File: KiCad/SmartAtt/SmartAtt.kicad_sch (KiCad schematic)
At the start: 11 parts, among them IC1 74LVC4245APW,112, J1 Conn_01x02_Pin, J2 Conn_01x02_Pin, J3 Conn_01x02_Pin, J4 Conn_01x04_Pin, U1 ESP32-WROOM-32E, U2 HMC542BLP4ETR, U3 MCP1703Ax-330xxDB

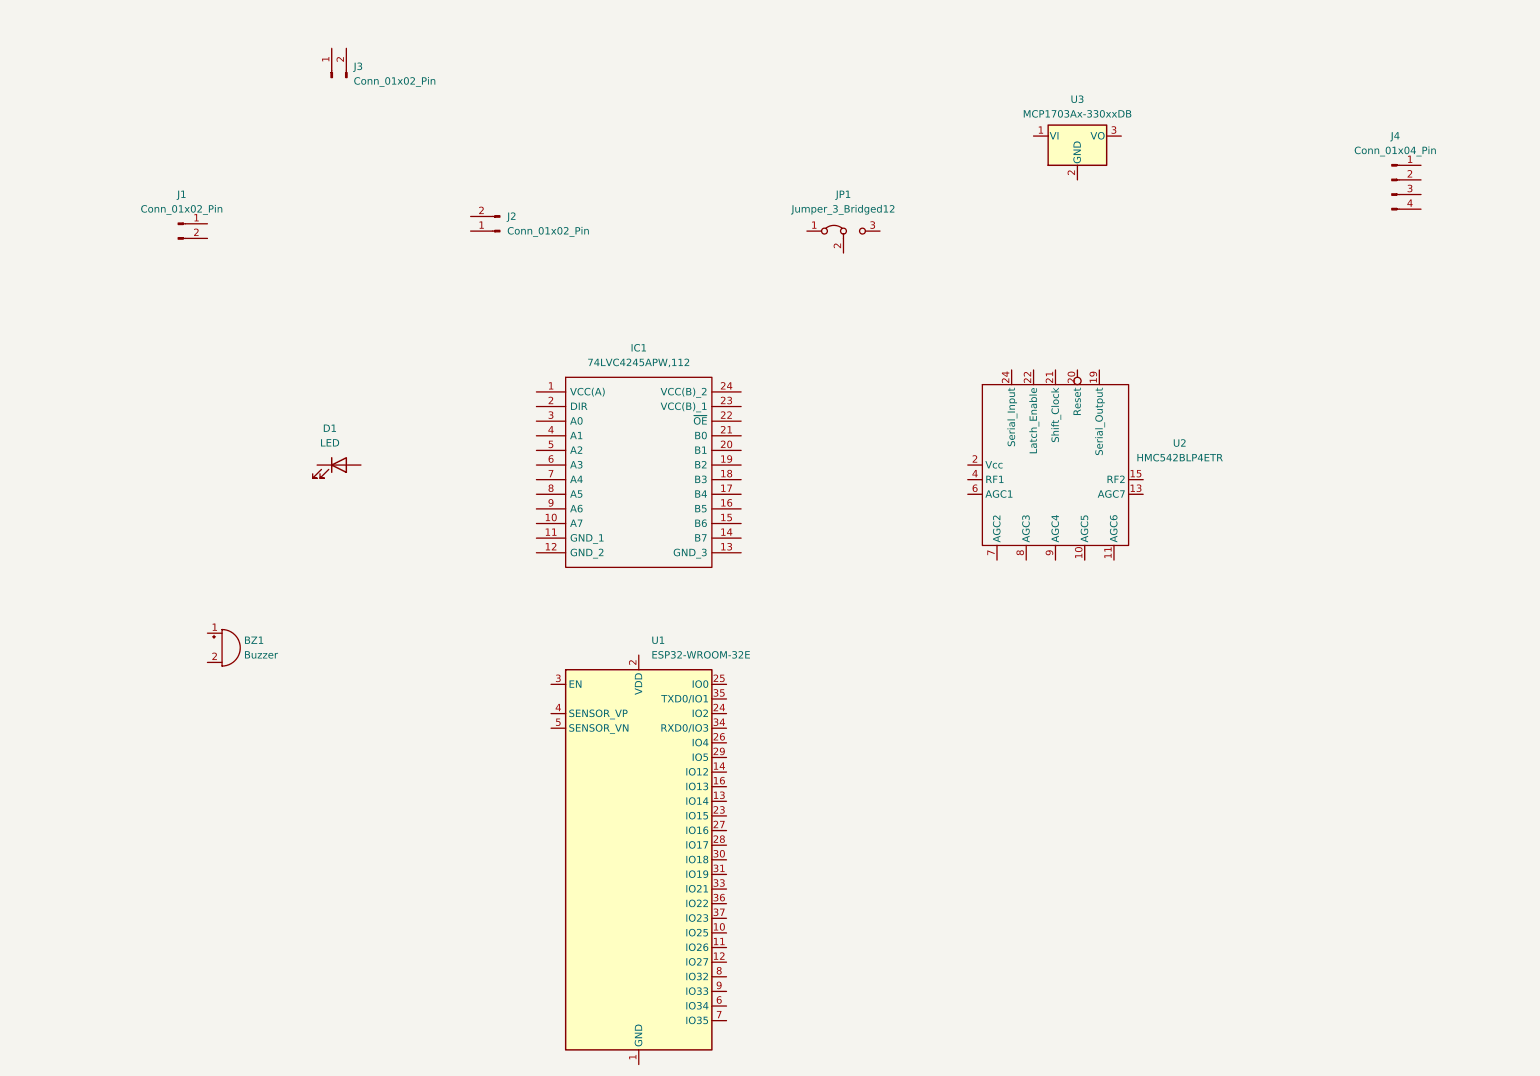
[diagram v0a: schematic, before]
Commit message: schematic finished. Need footprint to be added
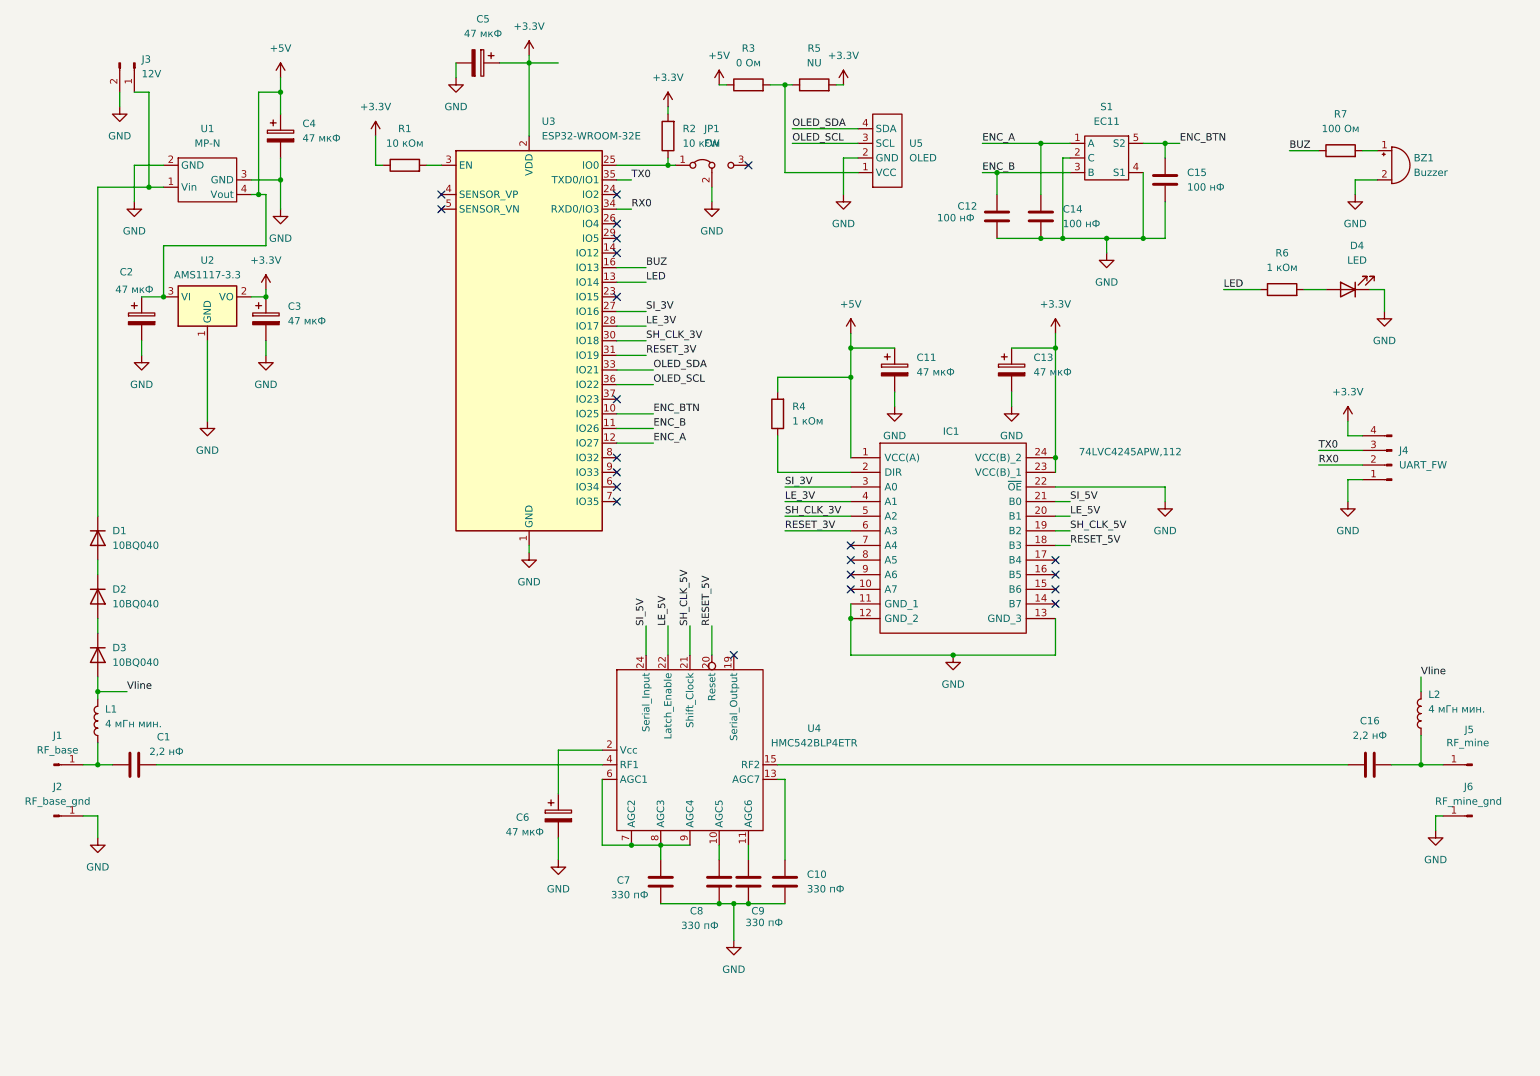
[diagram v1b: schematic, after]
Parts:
- removed J1, J2: Conn_01x02_Pin, symbol Connector:Conn_01x02_Pin
- removed U3: MCP1703Ax-330xxDB, Package_TO_SOT_SMD:SOT-223-3_TabPin2, symbol Regulator_Linear:MCP1703Ax-330xxDB
- added C1, C16: 2,2 нФ, symbol Device:C
- added C10, C7, C8, C9: 330 пФ, symbol Device:C
- added C11, C13, C2, C3, C4, C5, C6: 47 мкФ, symbol Device:C_Polarized
- added C12, C14, C15: 100 нФ, symbol Device:C
- added D1, D2, D3: 10BQ040, symbol Device:D
- added J1: RF_base, symbol Connector:Conn_01x01_Pin
- added J2: RF_base_gnd, symbol Connector:Conn_01x01_Pin
- added J5: RF_mine, symbol Connector:Conn_01x01_Pin
- added J6: RF_mine_gnd, symbol Connector:Conn_01x01_Pin
- added L1, L2: 4 мГн мин., symbol Device:L
- added R1, R2: 10 кОм, symbol Device:R
- added R3: 0 Ом, symbol Device:R
- added R4, R6: 1 кОм, symbol Device:R
- added R5: NU, symbol Device:R
- added R7: 100 Ом, symbol Device:R
- added S1: EC11, symbol Alexeyj4_Library:EC11_rotary_encoder
- added U1: MP-N, symbol Alexeyj4_Library:MPN
- added U2: AMS1117-3.3, Package_TO_SOT_SMD:SOT-223-3_TabPin2, symbol Regulator_Linear:AMS1117-3.3
- added U5: OLED, symbol Alexeyj4_Library:OLED I2C
- IC1: symbol Shar_Library:74LVC4245APW,112 -> Alexeyj4_Library:74LVC4245APW,112
- J3: value Conn_01x02_Pin -> 12V
- J4: value Conn_01x04_Pin -> UART_FW
- JP1: value Jumper_3_Bridged12 -> FW
- U4: renamed from U2; symbol Shar_Library:HMC542BLP4ETR -> Alexeyj4_Library:HMC542BLP4ETR
- renumbered D1 to D4, U1 to U3
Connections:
- net at BZ1.1 (+): now also R7.2
- net GND: now reaches BZ1.2 (-)
- net GND: now also D4.1 (K), IC1.11 (GND_1), IC1.12 (GND_2), IC1.13 (GND_3), IC1.22 (~{OE}), J3.2 (Pin_2), J4.1 (Pin_1), JP1.2 (C), U3.1 (GND), U3.15 (GND), U3.38 (GND), U3.39 (GND), C10.2, C11.2, C12.2, C13.2, C14.2, C15.2, C2.2, C3.2, C4.2, C5.2, C6.2, C7.2, C8.2, C9.2, J2.1 (Pin_1), J6.1 (Pin_1), S1.2 (C), S1.4 (S1), U1.2 (GND), U1.3 (GND), U2.1 (GND), U5.2 (GND)
- net at J3.1 (Pin_1): now also D1.1 (K), U1.1 (Vin)
- net RX0: now reaches J4.2 (Pin_2)
- net RX0: now also U3.34 (RXD0/IO3)
- net TX0: now reaches J4.3 (Pin_3)
- net TX0: now also U3.35 (TXD0/IO1)
- net +3.3V: now reaches J4.4 (Pin_4)
- net +3.3V: now also IC1.23 (VCC(B)_1), IC1.24 (VCC(B)_2), U3.2 (VDD), C13.1, C3.1, C5.1, R1.1, R2.2, R5.2, U2.2 (VO)
- net ENC_BTN: now reaches U3.10 (IO25)
- net ENC_BTN: now also C15.1, S1.5 (S2)
- net ENC_B: now reaches U3.11 (IO26)
- net ENC_B: now also C12.1, S1.3 (B)
- net ENC_A: now reaches U3.12 (IO27)
- net ENC_A: now also C14.1, S1.1 (A)
- net LED: now reaches U3.13 (IO14)
- net LED: now also R6.1
- net BUZ: now reaches U3.16 (IO13)
- net BUZ: now also R7.1
- net at U3.25 (IO0): now also JP1.1 (A), R2.1
- net SI_3V: now reaches U3.27 (IO16)
- net SI_3V: now also IC1.3 (A0)
- net LE_3V: now reaches U3.28 (IO17)
- net LE_3V: now also IC1.4 (A1)
- net at U3.3 (EN): now also R1.2
- net SH_CLK_3V: now reaches U3.30 (IO18)
- net SH_CLK_3V: now also IC1.5 (A2)
- net RESET_3V: now reaches U3.31 (IO19)
- net RESET_3V: now also IC1.6 (A3)
- net OLED_SDA: now reaches U3.33 (IO21)
- net OLED_SDA: now also U5.4 (SDA)
- net OLED_SCL: now reaches U3.36 (IO22)
- net OLED_SCL: now also U5.3 (SCL)
- net at D4.2 (A): now also R6.2
- net +5V: now reaches IC1.1 (VCC(A))
- net +5V: now also C11.1, C2.1, C4.1, R3.1, R4.2, U1.4 (Vout), U2.3 (VI)
- net RESET_5V: now reaches IC1.18 (B3)
- net RESET_5V: now also U4.20 (Reset)
- net SH_CLK_5V: now reaches IC1.19 (B2)
- net SH_CLK_5V: now also U4.21 (Shift_Clock)
- net at IC1.2 (DIR): now also R4.1
- net LE_5V: now reaches IC1.20 (B1)
- net LE_5V: now also U4.22 (Latch_Enable)
- net SI_5V: now reaches IC1.21 (B0)
- net SI_5V: now also U4.24 (Serial_Input)
- net at U4.10 (AGC5): now also C8.1
- net at U4.11 (AGC6): now also C9.1
- net at U4.13 (AGC7): now also C10.1
- net at U4.15 (RF2): now also C16.2
- net at U4.2 (Vcc): now also C6.1
- net at U4.4 (RF1): now also C1.1
- net at U4.6 (AGC1): now also U4.7 (AGC2), U4.8 (AGC3), U4.9 (AGC4), C7.1
- new net: D1.2 (A), D2.1 (K)
- new net: D2.2 (A), D3.1 (K)
- new net: C1.2, J1.1 (Pin_1), L1.1
- new net: C16.1, J5.1 (Pin_1), L2.1
- new net: R3.2, R5.1, U5.1 (VCC)
- new net Vline: D3.2 (A), L1.2, L2.2
- no-connect marks 0 -> 22
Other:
- moved on the sheet: BZ1, D4, IC1, J4, JP1, U3, U4

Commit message: contur added
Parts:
- BZ1: footprint (none) -> Alexeyj4:HC0903A
- C1, C16: footprint (none) -> Capacitor_THT:C_Disc_D10.0mm_W2.5mm_P5.00mm
- C10, C12, C14, C15, C7, C8, C9: footprint (none) -> Capacitor_SMD:C_0805_2012Metric_Pad1.18x1.45mm_HandSolder
- C11, C13, C2, C3, C4, C5, C6: footprint (none) -> Capacitor_Tantalum_SMD:CP_EIA-7343-31_Kemet-D_Pad2.25x2.55mm_HandSolder
- D1, D2, D3: footprint (none) -> Diode_SMD:D_SMB_Handsoldering
- D4: footprint (none) -> LED_SMD:LED_1206_3216Metric_Pad1.42x1.75mm_HandSolder
- J1, J2, J5, J6: footprint (none) -> TestPoint:TestPoint_Pad_1.0x1.0mm
- J3: footprint (none) -> Connector_JST:JST_PH_B2B-PH-K_1x02_P2.00mm_Vertical
- J4: footprint (none) -> Connector_PinHeader_2.54mm:PinHeader_1x04_P2.54mm_Vertical
- JP1: footprint (none) -> Connector_PinHeader_2.54mm:PinHeader_1x03_P2.54mm_Vertical
- L1, L2: footprint (none) -> Inductor_THT:L_Axial_L24.0mm_D7.1mm_P30.48mm_Horizontal_Vishay_IM-10-28
- R1, R2, R3, R4, R6, R7: footprint (none) -> Resistor_SMD:R_0805_2012Metric_Pad1.20x1.40mm_HandSolder
- R5: footprint (none) -> Resistor_SMD:R_0805_2012Metric_Pad1.20x1.40mm_HandSolder; now not fitted
- S1: footprint (none) -> Alexeyj4:RotaryEncoder EC11 SMD
- U1: footprint (none) -> Alexeyj4:MPN
- U5: footprint (none) -> Alexeyj4:OLED I2C
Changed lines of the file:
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@@
 			)
 		)
-		(property "Footprint" ""
+		(property "Footprint" "Capacitor_Tantalum_SMD:CP_EIA-7343-31_Kemet-D_Pad2.25x2.55mm_HandSolder"
 			(at 92.71 22.5552 0)
 			(effects
@@
 			)
 		)
-		(property "Footprint" ""
+		(property "Footprint" "Alexeyj4:HC0903A"
 			(at 254.635 36.83 90)
 			(effects
@@
 			)
 		)
-		(property "Footprint" ""
+		(property "Footprint" "Diode_SMD:D_SMB_Handsoldering"
 			(at 30.48 114.3 0)
 			(effects
@@
 			)
 		)
-		(property "Footprint" ""
+		(property "Footprint" "Resistor_SMD:R_0805_2012Metric_Pad1.20x1.40mm_HandSolder"
 			(at 246.38 38.608 90)
 			(effects
@@
 			)
 		)
-		(property "Footprint" ""
+		(property "Footprint" "Inductor_THT:L_Axial_L24.0mm_D7.1mm_P30.48mm_Horizontal_Vishay_IM-10-28"
 			(at 30.48 135.89 0)
 			(effects
@@
 			)
 		)
-		(property "Footprint" ""
+		(property "Footprint" "Resistor_SMD:R_0805_2012Metric_Pad1.20x1.40mm_HandSolder"
 			(at 236.22 62.738 90)
 			(effects
@@
 			)
 		)
-		(property "Footprint" ""
+		(property "Footprint" "Connector_PinHeader_2.54mm:PinHeader_1x04_P2.54mm_Vertical"
 			(at 255.27 91.44 0)
 			(effects
@@
 			)
 		)
-		(property "Footprint" ""
+		(property "Footprint" "Capacitor_Tantalum_SMD:CP_EIA-7343-31_Kemet-D_Pad2.25x2.55mm_HandSolder"
 			(at 169.8752 78.74 0)
 			(effects
@@
 			)
 		)
-		(property "Footprint" ""
+		(property "Footprint" "Capacitor_SMD:C_0805_2012Metric_Pad1.18x1.45mm_HandSolder"
 			(at 195.2752 52.07 0)
 			(effects
@@
 			)
 		)
-		(property "Footprint" ""
+		(property "Footprint" "Capacitor_THT:C_Disc_D10.0mm_W2.5mm_P5.00mm"
 			(at 247.65 144.4752 0)
 			(effects
@@
 			)
 		)
-		(property "Footprint" ""
+		(property "Footprint" "TestPoint:TestPoint_Pad_1.0x1.0mm"
 			(at 269.24 152.4 0)
 			(effects
@@
 			)
 		)
-		(property "Footprint" ""
+		(property "Footprint" "Capacitor_Tantalum_SMD:CP_EIA-7343-31_Kemet-D_Pad2.25x2.55mm_HandSolder"
 			(at 39.0652 69.85 0)
 			(effects
@@
 			)
 		)
-		(property "Footprint" ""
+		(property "Footprint" "Resistor_SMD:R_0805_2012Metric_Pad1.20x1.40mm_HandSolder"
 			(at 143.51 27.178 90)
 			(effects
@@
 			)
 		)
-		(property "Footprint" ""
+		(property "Footprint" "Capacitor_SMD:C_0805_2012Metric_Pad1.18x1.45mm_HandSolder"
 			(at 129.2352 167.64 0)
 			(effects
@@
 			)
 		)
-		(property "Footprint" ""
+		(property "Footprint" "Capacitor_SMD:C_0805_2012Metric_Pad1.18x1.45mm_HandSolder"
 			(at 144.4752 167.64 0)
 			(effects
@@
 			)
 		)
-		(property "Footprint" ""
+		(property "Footprint" "Diode_SMD:D_SMB_Handsoldering"
 			(at 30.48 124.46 0)
 			(effects
@@
 			)
 		)
-		(property "Footprint" ""
+		(property "Footprint" "Resistor_SMD:R_0805_2012Metric_Pad1.20x1.40mm_HandSolder"
 			(at 131.318 34.29 90)
 			(effects
@@
 			)
 		)
-		(property "Footprint" ""
+		(property "Footprint" "Capacitor_Tantalum_SMD:CP_EIA-7343-31_Kemet-D_Pad2.25x2.55mm_HandSolder"
 			(at 190.1952 78.74 0)
 			(effects
@@
 			)
 		)
-		(property "Footprint" ""
+		(property "Footprint" "Alexeyj4:RotaryEncoder EC11 SMD"
 			(at 205.74 38.1 0)
 			(effects
@@
 			)
 		)
-		(property "Footprint" ""
+		(property "Footprint" "TestPoint:TestPoint_Pad_1.0x1.0mm"
 			(at 269.24 143.51 0)
 			(effects
@@
 			)
 		)
-		(property "Footprint" ""
+		(property "Footprint" "Capacitor_Tantalum_SMD:CP_EIA-7343-31_Kemet-D_Pad2.25x2.55mm_HandSolder"
 			(at 60.6552 69.85 0)
 			(effects
@@
 			)
 		)
-		(property "Footprint" ""
+		(property "Footprint" "TestPoint:TestPoint_Pad_1.0x1.0mm"
 			(at 22.86 152.4 0)
 			(effects
@@
 			)
 		)
-		(property "Footprint" ""
+		(property "Footprint" "Resistor_SMD:R_0805_2012Metric_Pad1.20x1.40mm_HandSolder"
 			(at 150.368 82.55 90)
 			(effects
@@
 		(in_bom yes)
 		(on_board yes)
-		(dnp no)
+		(dnp yes)
 		(fields_autoplaced yes)
 		(property "Reference" "R5"
@@
 			)
 		)
-		(property "Footprint" ""
+		(property "Footprint" "Resistor_SMD:R_0805_2012Metric_Pad1.20x1.40mm_HandSolder"
 			(at 154.94 27.178 90)
 			(effects
@@
 			)
 		)
-		(property "Footprint" ""
+		(property "Footprint" "Capacitor_THT:C_Disc_D10.0mm_W2.5mm_P5.00mm"
 			(at 33.02 144.4752 0)
 			(effects
@@
 			)
 		)
-		(property "Footprint" ""
+		(property "Footprint" "Connector_PinHeader_2.54mm:PinHeader_1x03_P2.54mm_Vertical"
 			(at 137.16 39.37 0)
 			(effects
@@
 			)
 		)
-		(property "Footprint" ""
+		(property "Footprint" "LED_SMD:LED_1206_3216Metric_Pad1.42x1.75mm_HandSolder"
 			(at 247.65 60.96 0)
 			(effects
@@
 			)
 		)
-		(property "Footprint" ""
+		(property "Footprint" "Diode_SMD:D_SMB_Handsoldering"
 			(at 30.48 104.14 0)
 			(effects
@@
 			)
 		)
-		(property "Footprint" ""
+		(property "Footprint" "Resistor_SMD:R_0805_2012Metric_Pad1.20x1.40mm_HandSolder"
 			(at 83.82 41.148 90)
 			(effects
@@
 			)
 		)
-		(property "Footprint" ""
+		(property "Footprint" "Capacitor_SMD:C_0805_2012Metric_Pad1.18x1.45mm_HandSolder"
 			(at 139.3952 167.64 0)
 			(effects
@@
 			)
 		)
-		(property "Footprint" ""
+		(property "Footprint" "Capacitor_Tantalum_SMD:CP_EIA-7343-31_Kemet-D_Pad2.25x2.55mm_HandSolder"
 			(at 111.4552 156.21 0)
 			(effects
@@
 			)
 		)
-		(property "Footprint" ""
+		(property "Footprint" "Inductor_THT:L_Axial_L24.0mm_D7.1mm_P30.48mm_Horizontal_Vishay_IM-10-28"
 			(at 260.35 134.62 0)
 			(effects
@@
 			)
 		)
-		(property "Footprint" ""
+		(property "Footprint" "Capacitor_SMD:C_0805_2012Metric_Pad1.18x1.45mm_HandSolder"
 			(at 150.8252 167.64 0)
 			(effects
@@
 			)
 		)
-		(property "Footprint" ""
+		(property "Footprint" "Capacitor_SMD:C_0805_2012Metric_Pad1.18x1.45mm_HandSolder"
 			(at 187.6552 52.07 0)
 			(effects
@@
 			)
 		)
-		(property "Footprint" ""
+		(property "Footprint" "Connector_JST:JST_PH_B2B-PH-K_1x02_P2.00mm_Vertical"
 			(at 36.83 21.59 0)
 			(effects
@@
 			)
 		)
-		(property "Footprint" ""
+		(property "Footprint" "Alexeyj4:OLED I2C"
 			(at 167.64 36.83 0)
 			(effects
@@
 			)
 		)
-		(property "Footprint" ""
+		(property "Footprint" "Alexeyj4:MPN"
 			(at 49.53 41.91 0)
 			(effects
@@
 			)
 		)
-		(property "Footprint" ""
+		(property "Footprint" "Capacitor_SMD:C_0805_2012Metric_Pad1.18x1.45mm_HandSolder"
 			(at 216.8652 45.72 0)
 			(effects
@@
 			)
 		)
-		(property "Footprint" ""
+		(property "Footprint" "Capacitor_Tantalum_SMD:CP_EIA-7343-31_Kemet-D_Pad2.25x2.55mm_HandSolder"
 			(at 63.1952 38.1 0)
 			(effects
@@
 			)
 		)
-		(property "Footprint" ""
+		(property "Footprint" "TestPoint:TestPoint_Pad_1.0x1.0mm"
 			(at 22.86 143.51 0)
 			(effects
